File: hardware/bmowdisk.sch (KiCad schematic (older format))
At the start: 22 parts, among them CON1 IDC20, CON2 FL40YA-V36P-2X20-LF, CON3 FL40YA-V36P-2X20-LF, U1 SN74LVC8T245PW, U2 SN74LVC8T245PW, U3 SN74LVC8T245PW, U4 SN74LVC8T245PW

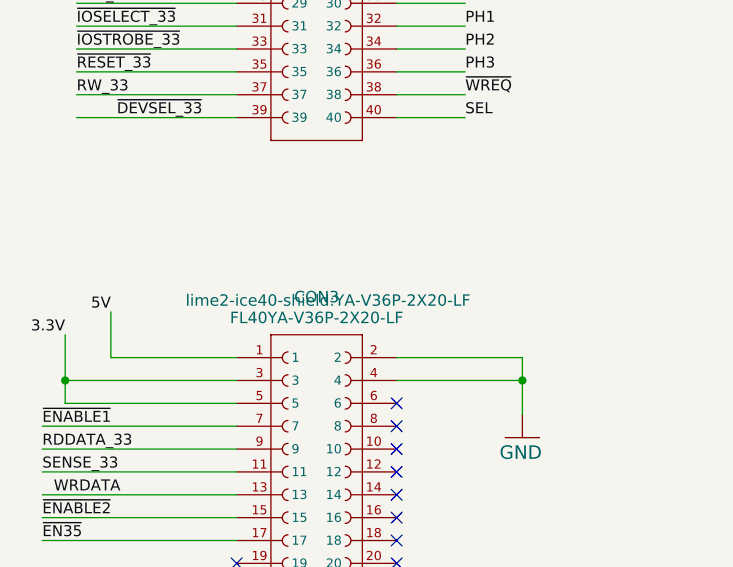
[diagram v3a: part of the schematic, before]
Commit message: Change resistor and cap footprints to 0805 for handsoldering
Signed-off-by: Rangel Ivanov <rangelivanov88@gmail.com>
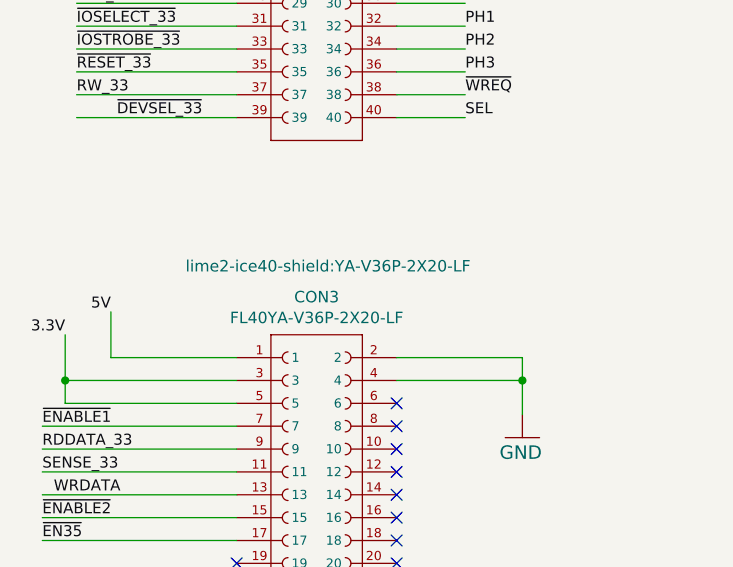
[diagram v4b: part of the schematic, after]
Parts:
- C1, C2, C3, C4, C5, C6, C7, C8: footprint bmowdisk:0805 -> bmowdisk:C_0805_2012Metric_Pad1.18x1.45mm_HandSolder
- R1, R2, R3, R4, R5, R6: footprint bmowdisk:0805 -> bmowdisk:R_0805_2012Metric_Pad1.20x1.40mm_HandSolder
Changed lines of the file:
@@
 F 0 "R2" H 10400 5409 59  0000 L BNN
 F 1 "390R" H 10400 5220 59  0000 L BNN
-F 2 "bmowdisk:0805" H 10550 5350 50  0001 C CNN
+F 2 "bmowdisk:R_0805_2012Metric_Pad1.20x1.40mm_HandSolder" H 10550 5350 50  0001 C CNN
 F 3 "" H 10550 5350 50  0001 C CNN
 	1    10550 5350
@@
 F 0 "CON3" H 2450 4635 50  0000 C CNN
 F 1 "FL40YA-V36P-2X20-LF" H 2450 4726 50  0000 C CNN
-F 2 "lime2-ice40-shield:YA-V36P-2X20-LF" H 2500 4650 50  0000 C CNN
+F 2 "lime2-ice40-shield:YA-V36P-2X20-LF" H 2500 4500 50  0000 C CNN
 F 3 "" H 2450 5900 60  0000 C CNN
 	1    2450 5900
@@
 F 0 "C5" H 7760 565 59  0000 L BNN
 F 1 "0.1uF" H 7760 365 59  0000 L BNN
-F 2 "bmowdisk:0805" H 7700 450 50  0001 C CNN
+F 2 "bmowdisk:C_0805_2012Metric_Pad1.18x1.45mm_HandSolder" H 7700 450 50  0001 C CNN
 F 3 "" H 7700 450 50  0001 C CNN
 	1    7700 450
@@
 F 0 "C1" H 6350 600 59  0000 L BNN
 F 1 "0.1uF" H 6200 350 59  0000 L BNN
-F 2 "bmowdisk:0805" H 6500 450 50  0001 C CNN
+F 2 "bmowdisk:C_0805_2012Metric_Pad1.18x1.45mm_HandSolder" H 6500 450 50  0001 C CNN
 F 3 "" H 6500 450 50  0001 C CNN
 	1    6500 450
@@
 F 0 "C2" H 6350 3300 59  0000 L BNN
 F 1 "0.1uF" H 6200 3050 59  0000 L BNN
-F 2 "bmowdisk:0805" H 6500 3150 50  0001 C CNN
+F 2 "bmowdisk:C_0805_2012Metric_Pad1.18x1.45mm_HandSolder" H 6500 3150 50  0001 C CNN
 F 3 "" H 6500 3150 50  0001 C CNN
 	1    6500 3150
@@
 F 0 "C6" H 7760 3265 59  0000 L BNN
 F 1 "0.1uF" H 7760 3065 59  0000 L BNN
-F 2 "bmowdisk:0805" H 7700 3150 50  0001 C CNN
+F 2 "bmowdisk:C_0805_2012Metric_Pad1.18x1.45mm_HandSolder" H 7700 3150 50  0001 C CNN
 F 3 "" H 7700 3150 50  0001 C CNN
 	1    7700 3150
@@
 F 0 "C3" H 6350 5750 59  0000 L BNN
 F 1 "0.1uF" H 6200 5500 59  0000 L BNN
-F 2 "bmowdisk:0805" H 6500 5600 50  0001 C CNN
+F 2 "bmowdisk:C_0805_2012Metric_Pad1.18x1.45mm_HandSolder" H 6500 5600 50  0001 C CNN
 F 3 "" H 6500 5600 50  0001 C CNN
 	1    6500 5600
@@
 F 0 "C7" H 7760 5715 59  0000 L BNN
 F 1 "0.1uF" H 7760 5515 59  0000 L BNN
-F 2 "bmowdisk:0805" H 7700 5600 50  0001 C CNN
+F 2 "bmowdisk:C_0805_2012Metric_Pad1.18x1.45mm_HandSolder" H 7700 5600 50  0001 C CNN
 F 3 "" H 7700 5600 50  0001 C CNN
 	1    7700 5600
@@
 F 0 "C4" H 6350 8200 59  0000 L BNN
 F 1 "0.1uF" H 6200 7950 59  0000 L BNN
-F 2 "bmowdisk:0805" H 6500 8050 50  0001 C CNN
+F 2 "bmowdisk:C_0805_2012Metric_Pad1.18x1.45mm_HandSolder" H 6500 8050 50  0001 C CNN
 F 3 "" H 6500 8050 50  0001 C CNN
 	1    6500 8050
@@
 F 0 "C8" H 7760 8165 59  0000 L BNN
 F 1 "0.1uF" H 7760 7965 59  0000 L BNN
-F 2 "bmowdisk:0805" H 7700 8050 50  0001 C CNN
+F 2 "bmowdisk:C_0805_2012Metric_Pad1.18x1.45mm_HandSolder" H 7700 8050 50  0001 C CNN
 F 3 "" H 7700 8050 50  0001 C CNN
 	1    7700 8050
@@
 F 0 "R5" H 8500 1009 59  0000 L BNN
 F 1 "22K" H 8500 820 59  0000 L BNN
-F 2 "bmowdisk:0805" H 8650 950 50  0001 C CNN
+F 2 "bmowdisk:R_0805_2012Metric_Pad1.20x1.40mm_HandSolder" H 8650 950 50  0001 C CNN
 F 3 "" H 8650 950 50  0001 C CNN
 	1    8650 950
@@
 F 0 "R6" H 8800 1009 59  0000 L BNN
 F 1 "22K" H 8800 820 59  0000 L BNN
-F 2 "bmowdisk:0805" H 8950 950 50  0001 C CNN
+F 2 "bmowdisk:R_0805_2012Metric_Pad1.20x1.40mm_HandSolder" H 8950 950 50  0001 C CNN
 F 3 "" H 8950 950 50  0001 C CNN
 	1    8950 950
@@
 F 0 "R1" H 4400 9459 59  0000 L BNN
 F 1 "2K2" H 4400 9270 59  0000 L BNN
-F 2 "bmowdisk:0805" H 4550 9400 50  0001 C CNN
+F 2 "bmowdisk:R_0805_2012Metric_Pad1.20x1.40mm_HandSolder" H 4550 9400 50  0001 C CNN
 F 3 "" H 4550 9400 50  0001 C CNN
 	1    4550 9400
@@
 F 0 "R3" H 4600 9909 59  0000 L BNN
 F 1 "3K3" H 4600 9720 59  0000 L BNN
-F 2 "bmowdisk:0805" H 4750 9850 50  0001 C CNN
+F 2 "bmowdisk:R_0805_2012Metric_Pad1.20x1.40mm_HandSolder" H 4750 9850 50  0001 C CNN
 F 3 "" H 4750 9850 50  0001 C CNN
 	1    4750 9850
@@
 F 0 "R4" H 5150 8909 59  0000 L BNN
 F 1 "22K" H 5150 8720 59  0000 L BNN
-F 2 "bmowdisk:0805" H 5300 8850 50  0001 C CNN
+F 2 "bmowdisk:R_0805_2012Metric_Pad1.20x1.40mm_HandSolder" H 5300 8850 50  0001 C CNN
 F 3 "" H 5300 8850 50  0001 C CNN
 	1    5300 8850

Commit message: Place and route board
Signed-off-by: Rangel Ivanov <rangelivanov88@gmail.com>
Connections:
- wire segments 215 -> 221
- no-connect marks 50 -> 44
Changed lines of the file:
@@
 Wire Wire Line
 	3400 1950 3450 1950
-NoConn ~ 2800 2150
 Wire Wire Line
 	2100 2050 1400 2050
@@
 Text Label 1400 1800 2    48   ~ 0
 3.3V
-Text Label 1400 2250 0    48   ~ 0
+Text Label 3100 2350 0    48   ~ 0
 A0_33
 Wire Wire Line
@@
 Wire Wire Line
 	2100 2650 1400 2650
-Text Label 1400 2350 0    48   ~ 0
+Text Label 3100 2450 0    48   ~ 0
 A1_33
-Text Label 1400 2450 0    48   ~ 0
+Text Label 3100 2550 0    48   ~ 0
 A2_33
-Text Label 1400 2550 0    48   ~ 0
+Text Label 3100 2650 0    48   ~ 0
 A3_33
-Text Label 1400 2650 0    48   ~ 0
+Text Label 3100 2750 0    48   ~ 0
 A4_33
 Wire Wire Line
@@
 Wire Wire Line
 	2100 2850 1400 2850
-Text Label 1400 2750 0    48   ~ 0
+Text Label 3100 2850 0    48   ~ 0
 A5_33
-Text Label 1400 2850 0    48   ~ 0
+Text Label 3100 2950 0    48   ~ 0
 A6_33
-Text Label 1400 2950 0    48   ~ 0
+Text Label 3100 3050 0    48   ~ 0
 A7_33
 Wire Wire Line
 	2100 2950 1400 2950
-Wire Wire Line
-	2100 3050 1400 3050
-Wire Wire Line
-	2100 3150 1400 3150
-Wire Wire Line
-	2100 3250 1400 3250
-Wire Wire Line
-	2100 3350 1400 3350
-Wire Wire Line
-	2100 3450 1400 3450
-Wire Wire Line
-	1400 3550 2100 3550
-Text Label 1400 3050 0    48   ~ 0
+Text Label 3100 3150 0    48   ~ 0
 A8_33
-Text Label 1400 3150 0    48   ~ 0
+Text Label 3100 3250 0    48   ~ 0
 A9_33
-Text Label 1400 3250 0    48   ~ 0
+Text Label 3100 3350 0    48   ~ 0
 A10_33
-Text Label 1400 3350 0    48   ~ 0
+Text Label 3100 3450 0    48   ~ 0
 A11_33
-Text Label 1400 3550 0    48   ~ 0
+Text Label 3000 5900 0    48   ~ 0
 ~IOSTROBE_33
-Wire Wire Line
-	2100 3650 1400 3650
-Wire Wire Line
-	2100 3750 1400 3750
 Wire Wire Line
 	1400 1800 1400 2050
@@
 Wire Wire Line
 	1400 2050 1400 2150
-Text Label 1400 3650 0    48   ~ 0
+Text Label 3050 6000 0    48   ~ 0
 ~RESET_33
-Text Label 1400 3750 0    48   ~ 0
+Text Label 3100 3850 0    48   ~ 0
 RW_33
-Wire Wire Line
-	2100 3850 1400 3850
-Text Label 1950 3850 2    48   ~ 0
+Text Label 3300 6300 2    48   ~ 0
 ~DEVSEL_33
-Text Label 3400 2250 2    48   ~ 0
+Text Label 1600 2250 2    48   ~ 0
 D0_33
 Wire Wire Line
@@
 Wire Wire Line
 	2800 2950 3400 2950
-Text Label 3400 2350 2    48   ~ 0
+Text Label 1600 2350 2    48   ~ 0
 D1_33
-Text Label 3400 2450 2    48   ~ 0
+Text Label 1600 2450 2    48   ~ 0
 D2_33
-Text Label 3400 2550 2    48   ~ 0
+Text Label 1600 2550 2    48   ~ 0
 D3_33
-Text Label 3400 2650 2    48   ~ 0
+Text Label 1600 2650 2    48   ~ 0
 D4_33
-Text Label 3400 2750 2    48   ~ 0
+Text Label 1600 2750 2    48   ~ 0
 D5_33
-Text Label 3400 2850 2    48   ~ 0
+Text Label 1600 2850 2    48   ~ 0
 D6_33
-Text Label 3400 2950 2    48   ~ 0
+Text Label 1600 2950 2    48   ~ 0
 D7_33
-Text Label 3000 3050 0    48   ~ 0
+Text Label 3100 3650 0    48   ~ 0
 Q3R_33
 Wire Wire Line
 	2800 3050 3400 3050
-Text Label 2950 3150 0    48   ~ 0
+Text Label 3100 3750 0    48   ~ 0
 7M_33
 Wire Wire Line
 	2800 3150 3400 3150
-Text Label 3400 3250 2    48   ~ 0
+Text Label 3400 2150 2    48   ~ 0
 EN245
 Wire Wire Line
 	2800 3250 3400 3250
-Text Label 3100 3350 0    48   ~ 0
+Text Label 3050 5100 0    48   ~ 0
 PH0
-Text Label 3100 3450 0    48   ~ 0
+Text Label 3050 5200 0    48   ~ 0
 PH1
 Wire Wire Line
@@
 Wire Wire Line
 	2800 3450 3100 3450
-Text Label 3100 3550 0    48   ~ 0
+Text Label 3050 5300 0    48   ~ 0
 PH2
 Wire Wire Line
@@
 Wire Wire Line
 	2800 3850 3100 3850
-Text Label 3100 3650 0    48   ~ 0
+Text Label 3050 5400 0    48   ~ 0
 PH3
-Text Label 3100 3750 0    48   ~ 0
+Text Label 3050 5500 0    48   ~ 0
 ~WREQ
-Text Label 3100 3850 0    48   ~ 0
+Text Label 3050 5600 0    48   ~ 0
 SEL
 $Comp
@@
 	1    0    0    1
 $EndComp
-Text Label 1250 5200 0    48   ~ 0
+Text Label 3050 5700 0    48   ~ 0
 ~ENABLE1
 Wire Wire Line
 	2100 5200 1250 5200
-Text Label 1250 5300 0    48   ~ 0
+Text Label 3050 6200 0    48   ~ 0
 RDDATA_33
 Wire Wire Line
 	2100 5300 1250 5300
-Text Label 1250 5400 0    48   ~ 0
+Text Label 3050 6100 0    48   ~ 0
 SENSE_33
-Wire Wire Line
-	2100 5400 1250 5400
 Connection ~ 3400 1950
 NoConn ~ 11050 5050
@@
 NoConn ~ 2100 6700
 NoConn ~ 2100 6800
-NoConn ~ 2800 5200
-NoConn ~ 2800 5300
-NoConn ~ 2800 5400
-NoConn ~ 2800 5500
-NoConn ~ 2800 5600
-NoConn ~ 2800 5700
-NoConn ~ 2800 5800
-NoConn ~ 2800 5900
-NoConn ~ 2800 6000
-NoConn ~ 2800 6100
-NoConn ~ 2800 6200
-NoConn ~ 2800 6300
-NoConn ~ 2800 6400
-NoConn ~ 2800 6500
-NoConn ~ 2800 6600
-NoConn ~ 2800 6700
-NoConn ~ 2800 6800
-Text Label 1300 5500 0    48   ~ 0
+Text Label 3050 5800 0    48   ~ 0
 WRDATA
-Wire Wire Line
-	1250 5500 2100 5500
-Text Label 1250 5600 0    48   ~ 0
+Text Label 1250 5200 0    48   ~ 0
 ~ENABLE2
-Wire Wire Line
-	1250 5600 2100 5600
-Text Label 1250 5700 0    48   ~ 0
+Text Label 1250 5300 0    48   ~ 0
 ~EN35
-Wire Wire Line
-	1250 5700 2100 5700
 Wire Wire Line
 	2100 4900 1550 4900
@@
 Text Label 1550 4700 2    48   ~ 0
 5V
-NoConn ~ 2800 5100
 Wire Wire Line
 	2800 4900 3350 4900
@@
 Text Label 8950 550  0    48   ~ 0
 5V
+Text Label 6000 9200 0    48   ~ 0
+D7_33
+Text Label 6000 9100 0    48   ~ 0
+D6_33
+Text Label 6000 9000 0    48   ~ 0
+D5_33
+Text Label 6000 8900 0    48   ~ 0
+D4_33
+Text Label 6000 8800 0    48   ~ 0
+D3_33
+Text Label 6000 8700 0    48   ~ 0
+D2_33
+Text Label 6000 8600 0    48   ~ 0
+D1_33
 Text Label 6000 8500 0    48   ~ 0
-D7_33
-Text Label 6000 8600 0    48   ~ 0
-D6_33
-Text Label 6000 8700 0    48   ~ 0
-D5_33
-Text Label 6000 8800 0    48   ~ 0
-D4_33
-Text Label 6000 8900 0    48   ~ 0
-D3_33
-Text Label 6000 9000 0    48   ~ 0
-D2_33
-Text Label 6000 9100 0    48   ~ 0
-D1_33
-Text Label 6000 9200 0    48   ~ 0
 D0_33
-Text Label 7850 8500 0    48   ~ 0
+Text Label 7900 9200 0    48   ~ 0
 D7
-Text Label 7850 8600 0    48   ~ 0
+Text Label 7900 9100 0    48   ~ 0
 D6
-Text Label 7850 8700 0    48   ~ 0
+Text Label 7900 9000 0    48   ~ 0
 D5
-Text Label 7850 8800 0    48   ~ 0
+Text Label 7900 8900 0    48   ~ 0
 D4
-Text Label 7850 8900 0    48   ~ 0
+Text Label 7900 8800 0    48   ~ 0
 D3
-Text Label 7850 9000 0    48   ~ 0
+Text Label 7900 8700 0    48   ~ 0
 D2
-Text Label 7850 9100 0    48   ~ 0
+Text Label 7900 8600 0    48   ~ 0
 D1
-Text Label 7850 9200 0    48   ~ 0
+Text Label 7900 8500 0    48   ~ 0
 D0
 Text Label 6000 9500 0    48   ~ 0
@@
 Text Label 5300 8650 2    48   ~ 0
 3.3V
-Text Label 1400 3450 0    48   ~ 0
+Text Label 3100 2250 0    48   ~ 0
 ~IOSELECT_33
 Text Label 7750 1500 0    48   ~ 0
 ~RESET
+Wire Wire Line
+	2800 5100 3050 5100
+Wire Wire Line
+	2800 5200 3050 5200
+Wire Wire Line
+	2800 5300 3050 5300
+Wire Wire Line
+	2800 5400 3050 5400
+Wire Wire Line
+	2800 5500 3050 5500
+Wire Wire Line
+	2800 5600 3050 5600
+Wire Wire Line
+	2800 5700 3050 5700
+Wire Wire Line
+	2800 5800 3050 5800
+Wire Wire Line
+	2800 6000 3050 6000
+Wire Wire Line
+	2800 6100 3050 6100
+Wire Wire Line
+	2800 6200 3050 6200
+Wire Wire Line
+	2800 2150 3400 2150
+Wire Wire Line
+	2800 6400 3050 6400
+Wire Wire Line
+	2800 6700 3050 6700
+Wire Wire Line
+	2800 6800 3050 6800
+Wire Wire Line
+	2800 6600 3250 6600
+Wire Wire Line
+	2800 6500 3250 6500
+Wire Wire Line
+	2800 6300 3300 6300
+Wire Wire Line
+	2800 5900 3250 5900
+NoConn ~ 2100 3050
+NoConn ~ 2100 3150
+NoConn ~ 2100 3250
+NoConn ~ 2100 3350
+NoConn ~ 2100 3450
+NoConn ~ 2100 3550
+NoConn ~ 2100 3650
+NoConn ~ 2100 3750
+NoConn ~ 2100 3850
+NoConn ~ 2100 5400
+NoConn ~ 2100 5500
+NoConn ~ 2100 5600
+NoConn ~ 2100 5700
 $EndSCHEMATC

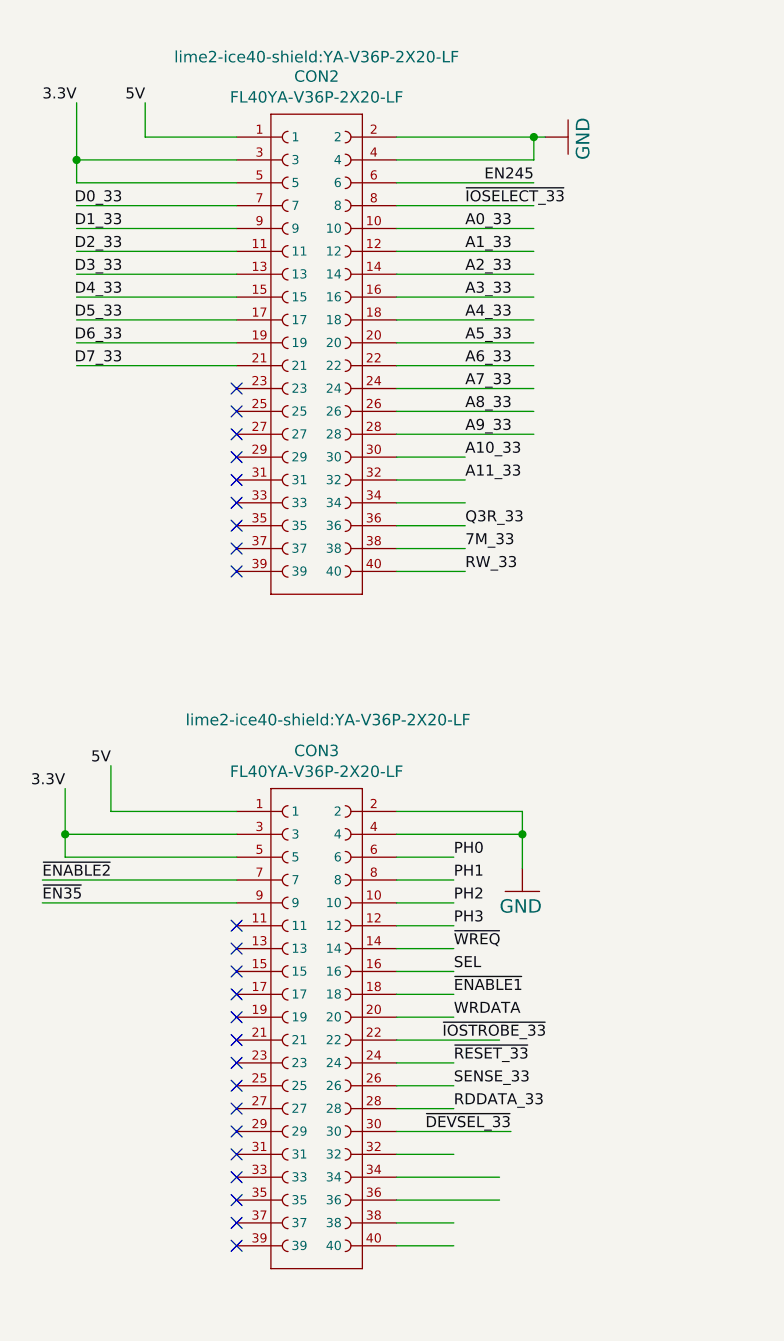
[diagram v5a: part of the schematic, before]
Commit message: Fix connections to 0.05 inch headers
Signed-off-by: Rangel Ivanov <rangelivanov88@gmail.com>
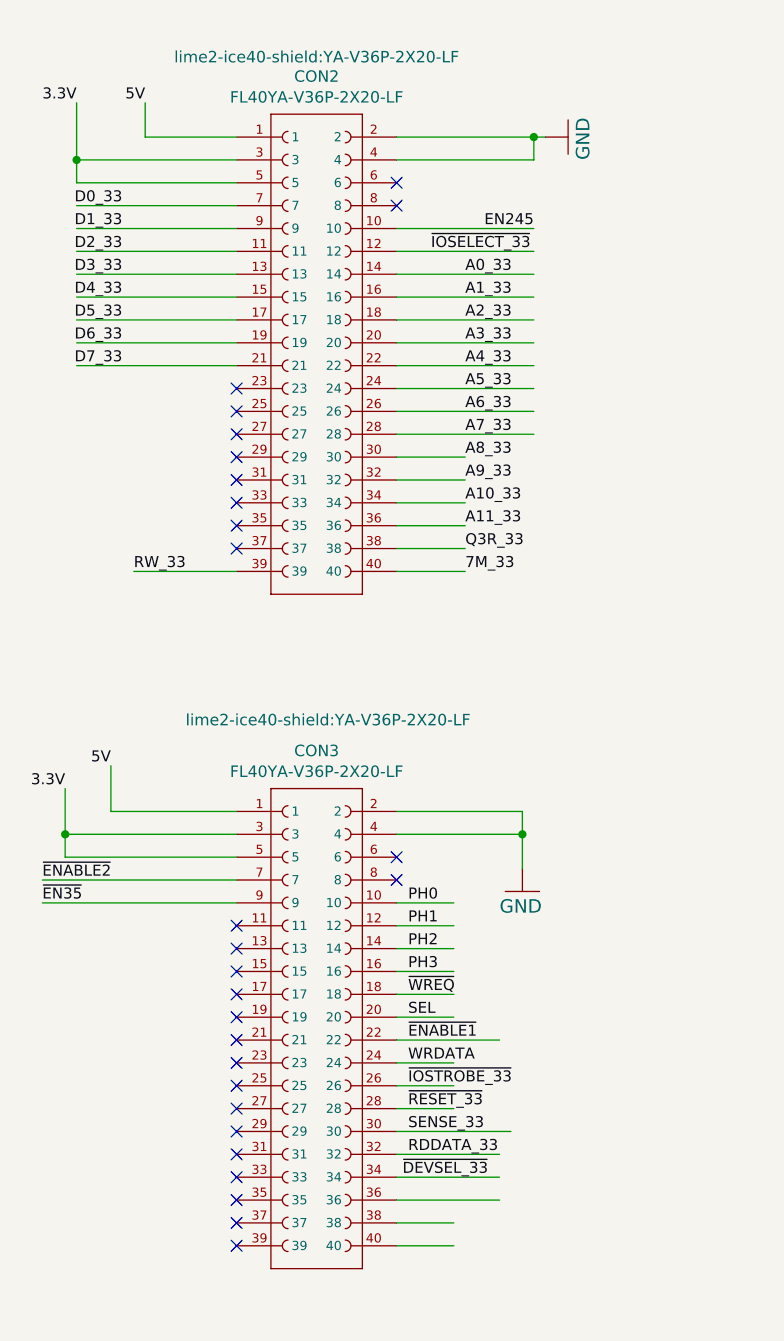
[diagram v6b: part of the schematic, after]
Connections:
- wire segments 221 -> 218
- no-connect marks 44 -> 47
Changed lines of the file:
@@
 Text Label 1400 1800 2    48   ~ 0
 3.3V
-Text Label 3100 2350 0    48   ~ 0
+Text Label 3100 2550 0    48   ~ 0
 A0_33
 Wire Wire Line
@@
 Wire Wire Line
 	2100 2650 1400 2650
-Text Label 3100 2450 0    48   ~ 0
+Text Label 3100 2650 0    48   ~ 0
 A1_33
-Text Label 3100 2550 0    48   ~ 0
+Text Label 3100 2750 0    48   ~ 0
 A2_33
-Text Label 3100 2650 0    48   ~ 0
+Text Label 3100 2850 0    48   ~ 0
 A3_33
-Text Label 3100 2750 0    48   ~ 0
+Text Label 3100 2950 0    48   ~ 0
 A4_33
 Wire Wire Line
@@
 Wire Wire Line
 	2100 2850 1400 2850
-Text Label 3100 2850 0    48   ~ 0
+Text Label 3100 3050 0    48   ~ 0
 A5_33
-Text Label 3100 2950 0    48   ~ 0
+Text Label 3100 3150 0    48   ~ 0
 A6_33
-Text Label 3100 3050 0    48   ~ 0
+Text Label 3100 3250 0    48   ~ 0
 A7_33
 Wire Wire Line
 	2100 2950 1400 2950
-Text Label 3100 3150 0    48   ~ 0
+Text Label 3100 3350 0    48   ~ 0
 A8_33
-Text Label 3100 3250 0    48   ~ 0
+Text Label 3100 3450 0    48   ~ 0
 A9_33
-Text Label 3100 3350 0    48   ~ 0
+Text Label 3100 3550 0    48   ~ 0
 A10_33
-Text Label 3100 3450 0    48   ~ 0
+Text Label 3100 3650 0    48   ~ 0
 A11_33
-Text Label 3000 5900 0    48   ~ 0
+Text Label 2850 6100 0    48   ~ 0
 ~IOSTROBE_33
 Wire Wire Line
@@
 Wire Wire Line
 	1400 2050 1400 2150
-Text Label 3050 6000 0    48   ~ 0
+Text Label 2850 6200 0    48   ~ 0
 ~RESET_33
-Text Label 3100 3850 0    48   ~ 0
+Text Label 1650 3850 0    48   ~ 0
 RW_33
-Text Label 3300 6300 2    48   ~ 0
+Text Label 3200 6500 2    48   ~ 0
 ~DEVSEL_33
 Text Label 1600 2250 2    48   ~ 0
 D0_33
-Wire Wire Line
-	2800 2250 3400 2250
 Wire Wire Line
 	2800 2350 3400 2350
@@
 Text Label 1600 2950 2    48   ~ 0
 D7_33
-Text Label 3100 3650 0    48   ~ 0
+Text Label 3100 3750 0    48   ~ 0
 Q3R_33
 Wire Wire Line
 	2800 3050 3400 3050
-Text Label 3100 3750 0    48   ~ 0
+Text Label 3100 3850 0    48   ~ 0
 7M_33
 Wire Wire Line
 	2800 3150 3400 3150
-Text Label 3400 2150 2    48   ~ 0
+Text Label 3400 2350 2    48   ~ 0
 EN245
 Wire Wire Line
 	2800 3250 3400 3250
-Text Label 3050 5100 0    48   ~ 0
+Text Label 2850 5300 0    48   ~ 0
 PH0
-Text Label 3050 5200 0    48   ~ 0
+Text Label 2850 5400 0    48   ~ 0
 PH1
 Wire Wire Line
@@
 Wire Wire Line
 	2800 3450 3100 3450
-Text Label 3050 5300 0    48   ~ 0
+Text Label 2850 5500 0    48   ~ 0
 PH2
 Wire Wire Line
@@
 Wire Wire Line
 	2800 3850 3100 3850
-Text Label 3050 5400 0    48   ~ 0
+Text Label 2850 5600 0    48   ~ 0
 PH3
-Text Label 3050 5500 0    48   ~ 0
+Text Label 2850 5700 0    48   ~ 0
 ~WREQ
-Text Label 3050 5600 0    48   ~ 0
+Text Label 2850 5800 0    48   ~ 0
 SEL
 $Comp
@@
 	1    0    0    1
 $EndComp
-Text Label 3050 5700 0    48   ~ 0
+Text Label 2850 5900 0    48   ~ 0
 ~ENABLE1
 Wire Wire Line
 	2100 5200 1250 5200
-Text Label 3050 6200 0    48   ~ 0
+Text Label 2850 6400 0    48   ~ 0
 RDDATA_33
 Wire Wire Line
 	2100 5300 1250 5300
-Text Label 3050 6100 0    48   ~ 0
+Text Label 2850 6300 0    48   ~ 0
 SENSE_33
 Connection ~ 3400 1950
@@
 NoConn ~ 2100 6700
 NoConn ~ 2100 6800
-Text Label 3050 5800 0    48   ~ 0
+Text Label 2850 6000 0    48   ~ 0
 WRDATA
 Text Label 1250 5200 0    48   ~ 0
@@
 Text Label 5300 8650 2    48   ~ 0
 3.3V
-Text Label 3100 2250 0    48   ~ 0
+Text Label 2950 2450 0    48   ~ 0
 ~IOSELECT_33
 Text Label 7750 1500 0    48   ~ 0
 ~RESET
 Wire Wire Line
-	2800 5100 3050 5100
-Wire Wire Line
-	2800 5200 3050 5200
-Wire Wire Line
 	2800 5300 3050 5300
 Wire Wire Line
@@
 Wire Wire Line
 	2800 6200 3050 6200
-Wire Wire Line
-	2800 2150 3400 2150
-Wire Wire Line
-	2800 6400 3050 6400
 Wire Wire Line
 	2800 6700 3050 6700
@@
 NoConn ~ 2100 3650
 NoConn ~ 2100 3750
-NoConn ~ 2100 3850
 NoConn ~ 2100 5400
 NoConn ~ 2100 5500
 NoConn ~ 2100 5600
 NoConn ~ 2100 5700
+Wire Wire Line
+	2100 3850 1650 3850
+NoConn ~ 2800 2150
+NoConn ~ 2800 2250
+Wire Wire Line
+	2800 6400 3250 6400
+NoConn ~ 2800 5100
+NoConn ~ 2800 5200
 $EndSCHEMATC
